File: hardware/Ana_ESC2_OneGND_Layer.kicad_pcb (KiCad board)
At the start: 4 copper layers, 90 x 90 mm, 110 parts, among them IC1 TCAN330DCNT, J1 BM04B-GHS-TBT_LF__SN__N_, J2 USB_C_Receptacle_USB2.0_16P, J3 Conn_01x02_Socket, J4 Conn_01x04_Pin, J5 BM04B-GHS-TBT_LF__SN__N_, Q10 STL90N6F7, Q11 STL90N6F7, Q12 STL90N6F7, Q7 STL90N6F7, Q8 STL90N6F7, Q9 STL90N6F7, SW1 SW_SPDT, SW2 SW_SPDT, U1 DRV8323RSRGZR, U2 ME6211C33M5, U3 STM32G431CBU6, Y1 ECS-80-20-5PX-TR

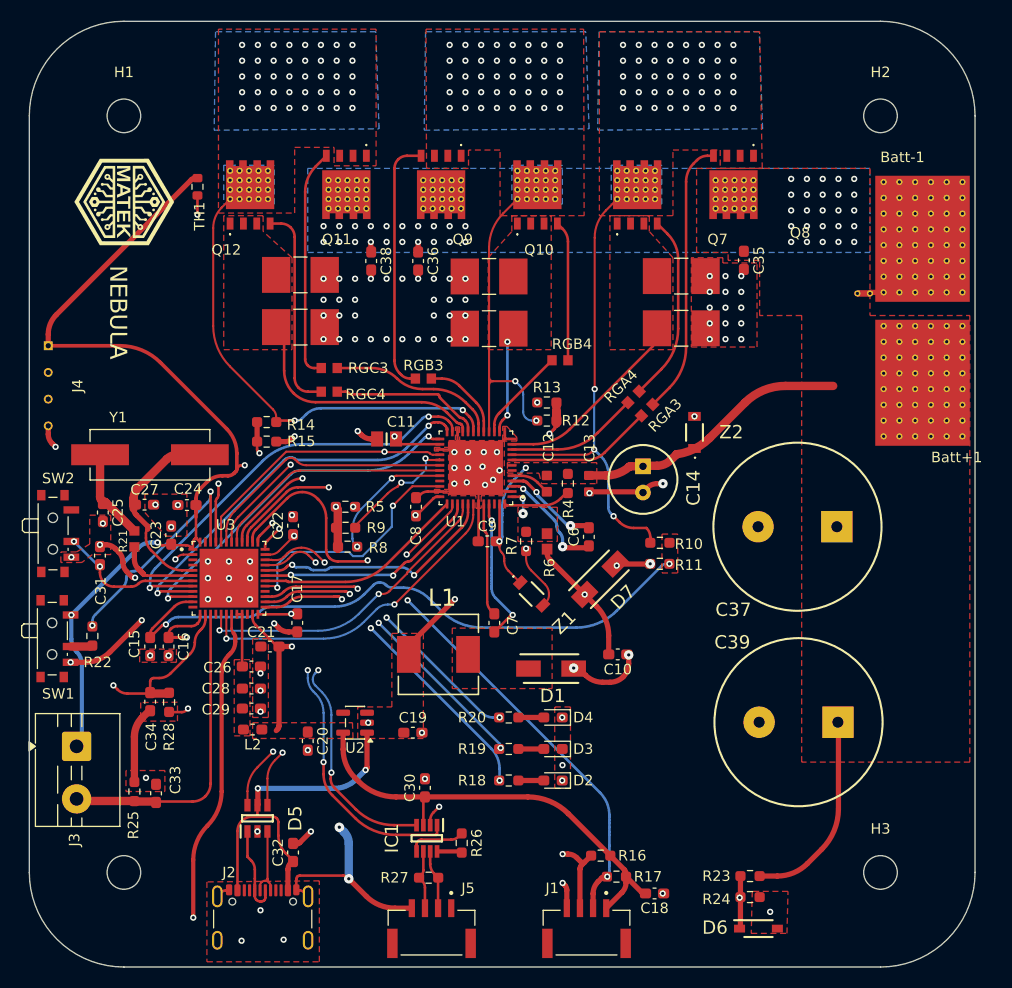
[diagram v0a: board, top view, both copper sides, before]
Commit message: After graduation presantition. USB differantial ways improved for usb connection issue. DRV83233 Enable and nSCS pins changed to be in true connection with STM32G431. ETC
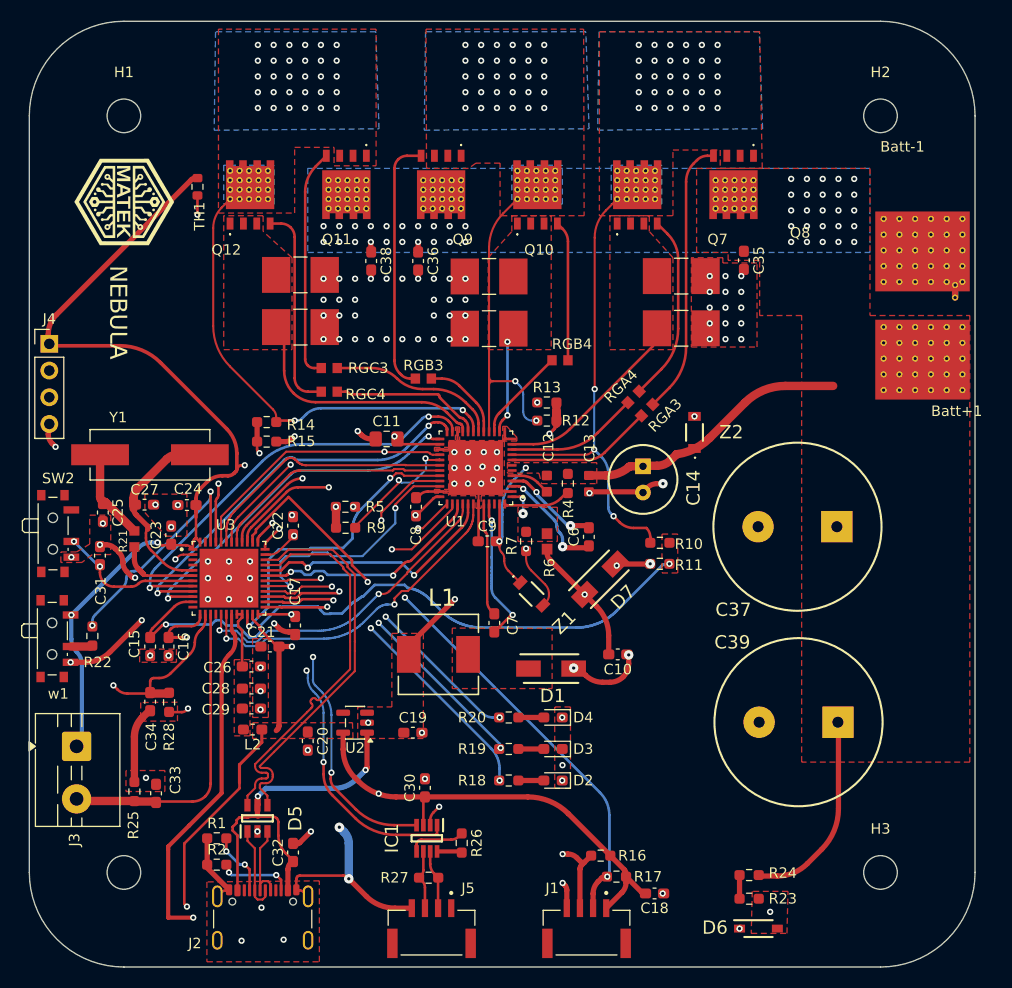
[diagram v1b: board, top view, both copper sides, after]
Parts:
- removed R8: 10k, Resistor_SMD:R_0603_1608Metric_Pad0.98x0.95mm_HandSolder
- added R1: 5.1k, Resistor_SMD:R_0603_1608Metric_Pad0.98x0.95mm_HandSolder, F.Cu at (66.3, 129.2)
- added R2: 5.1k, Resistor_SMD:R_0603_1608Metric_Pad0.98x0.95mm_HandSolder, F.Cu at (66.3, 131.8)
- C11: footprint 08056D104KAT2A:CAPC2012X140N -> Capacitor_SMD:C_0805_2012Metric_Pad1.18x1.45mm_HandSolder
- J4: footprint Connector_PinHeader_1.00mm:PinHeader_1x04_P1.00mm_Vertical -> Connector_PinHeader_2.54mm:PinHeader_1x04_P2.54mm_Vertical
- moved J4 10.3 mm to (50.4, 82.2)
- moved NT1 8.14 mm to (136.6, 76.6), turned to -90 degrees
- moved Batt+1 4.40 mm to (133.8, 80.1)
- moved R23 2.16 mm to (117.0, 135.0), turned to 0 degrees
- moved R24 2.10 mm to (117.0, 132.8), turned to 180 degrees
- moved Batt-1 1.00 mm to (133.8, 69.8)
- moved C17 0.32 mm to (73.8, 109.0)
- renumbered SW1 to w1
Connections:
- J2 pad A5: unconnected-(J2-CC1-PadA5) -> Net-(J2-CC1)
- J2 pad B5: unconnected-(J2-CC2-PadB5) -> Net-(J2-CC2)
- R23 pad 1: VM -> Net-(R23-Pad1)
- R23 pad 2: /MCU/VBus -> GND2
- R24 pad 1: /MCU/VBus -> VM
- R24 pad 2: GND2 -> Net-(R23-Pad1)
- U1 pad 32: Net-(U1-SCS_N) -> /Gate_Driver/nSCS
- U3 pad 22: unconnected-(U3-PB10-Pad22) -> /Gate_Driver/nSCS
- U3 pad 28: unconnected-(U3-PB15-Pad28) -> /Gate_Driver/Enable
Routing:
- net +3.3V: track 185.6 -> 259.3 mm, vias 6 -> 8
- net /Gate_Driver/Enable: track 0.00 -> 30.7 mm, vias 0 -> 2
- net /Gate_Driver/nSCS: track 0.00 -> 29.3 mm, vias 0 -> 2
- net /MCU/UART_P: track 51.9 -> 72.4 mm
- net /MCU/UART_N: track 50.2 -> 64.9 mm
- net Net-(U1-SCS_N): track 12.7 -> 0.00 mm, vias 2 -> 0
- net /Gate_Driver/INHA: track 20.2 -> 31.8 mm, vias 0 -> 2
- net Net-(J2-CC2): track 0.00 -> 7.09 mm, vias 0 -> 2
- net Net-(J2-CC1): track 0.00 -> 6.16 mm, vias 0 -> 2
- net GND2: track 63.2 -> 69.0 mm
- net /MCU/USB_DN: track 32.1 -> 37.7 mm, vias 2 -> 0
- net /MCU/USB_DP: track 32.3 -> 37.8 mm, vias 2 -> 0
- net /Gate_Driver/SENS1: track 60.0 -> 62.7 mm
- net Net-(R23-Pad1): track 0.00 -> 2.25 mm
- net /Gate_Driver/DVDD: track 16.0 -> 13.8 mm
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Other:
- board text added: "ABDEL MANAN ABDEL RAHMAN ALPEREN ŞAHİN 2026/07"
- board text removed: "ABDEL MANAN ABDEL RAHMAN ALPEREN ŞAHİN 2026/05"
